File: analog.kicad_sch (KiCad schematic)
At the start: 38 parts, among them J3 Conn_02x01, J4 Conn_02x01, J5 Conn_02x01, J6 Conn_02x01, J7 Screw_Terminal_01x02, U4 ADS131A04, Y2 16.384 MHz

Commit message: June 20th is not real and cant hurt me
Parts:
- C20: renamed from C15; footprint aprlprints:C_0603-noct -> APRLPrints:C_0603
- C21: renamed from C46; footprint aprlprints:C_0603-noct -> APRLPrints:C_0603
- C22: renamed from C16; footprint aprlprints:C_0603-noct -> APRLPrints:C_0603
- C23: renamed from C17; footprint aprlprints:C_0603-noct -> APRLPrints:C_0603
- C24: renamed from C18; footprint aprlprints:C_0603-noct -> APRLPrints:C_0603
- C25: renamed from C19; footprint aprlprints:C_0603-noct -> APRLPrints:C_0603
- C26: renamed from C20; footprint aprlprints:C_0603-noct -> APRLPrints:C_0603
- C27: renamed from C21; footprint aprlprints:C_0603-noct -> APRLPrints:C_0603
- C28: renamed from C22; footprint aprlprints:C_0603-noct -> APRLPrints:C_0603
- C29: renamed from C23; footprint aprlprints:C_0603-noct -> APRLPrints:C_0603
- C30: renamed from C24; footprint aprlprints:C_0603-noct -> APRLPrints:C_0603
- C31: renamed from C25; footprint aprlprints:C_0603-noct -> APRLPrints:C_0603
- C32: renamed from C26; footprint aprlprints:C_0603-noct -> APRLPrints:C_0603
- C33: renamed from C27; footprint aprlprints:C_0603-noct -> APRLPrints:C_0603
- F2: footprint Fuse:Fuse_0805_2012Metric -> APRLPrints:Fuse_0805_2012Metric
- Y2: footprint aprlprints:3225-4P-L-noct -> APRLPrints:3225-4P-L
- renumbered U4 to U5

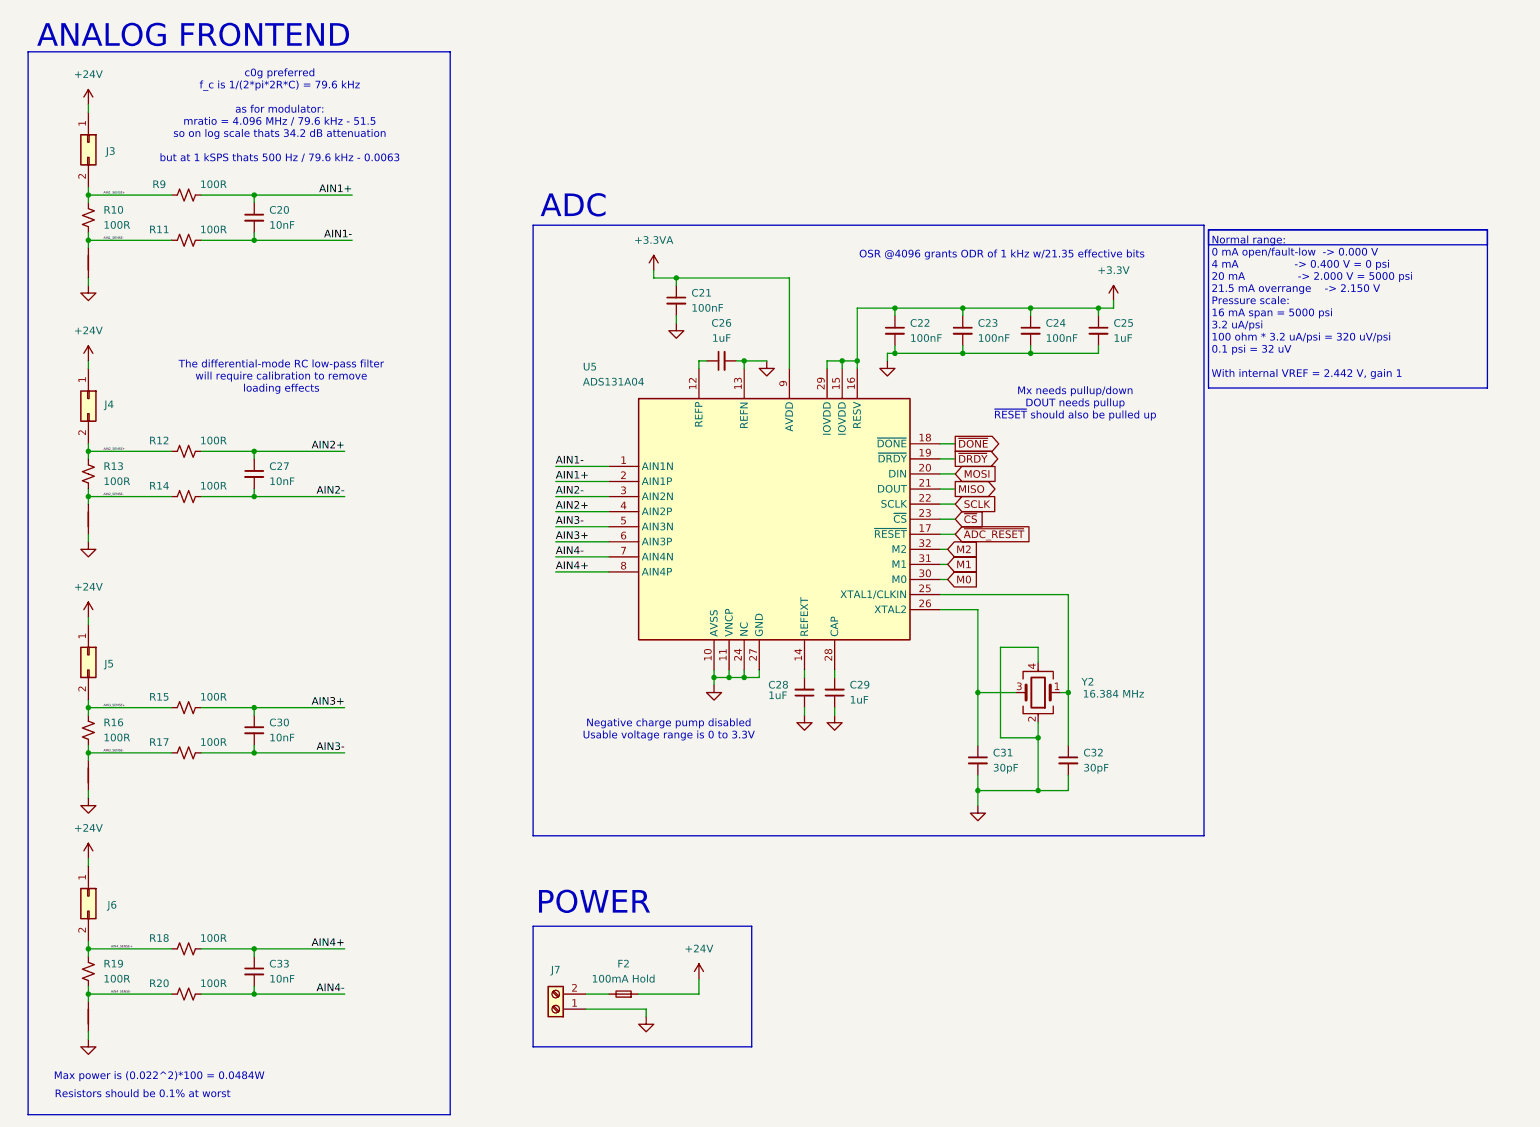
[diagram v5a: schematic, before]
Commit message: Remove LP5907
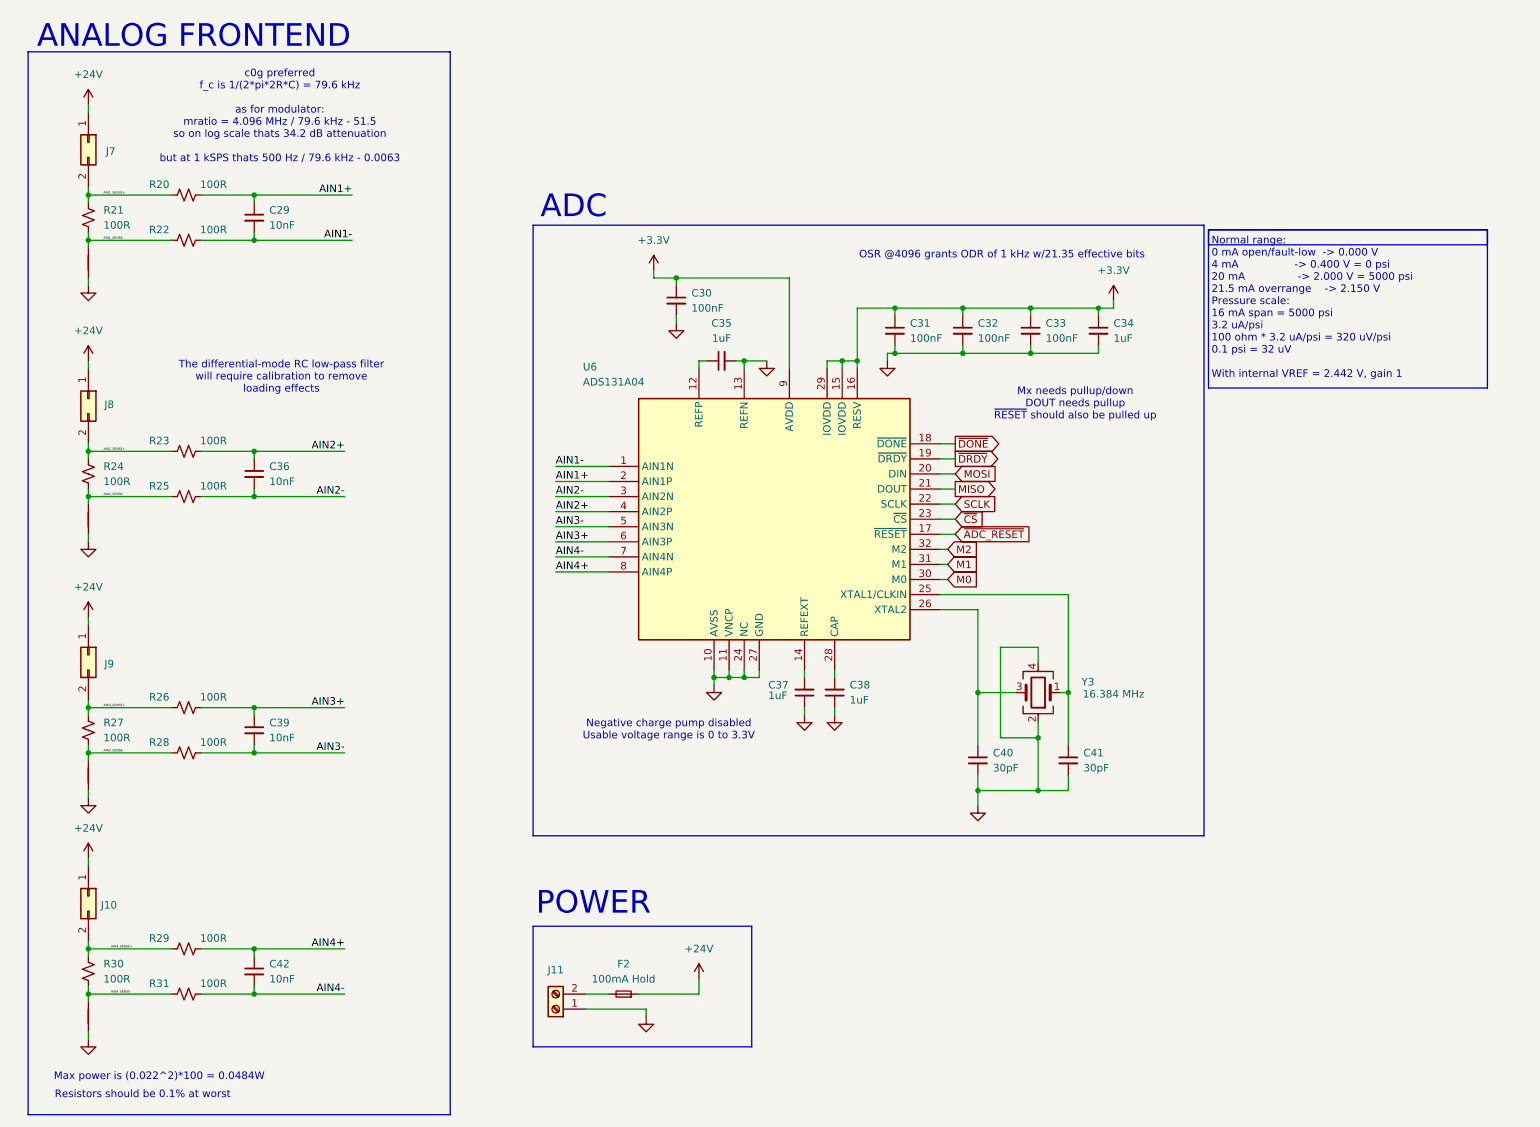
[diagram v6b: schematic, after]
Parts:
- renumbered C20 to C29, C21 to C30, C22 to C31, C23 to C32, C24 to C33, C25 to C34, C26 to C35, C27 to C36, C28 to C37, C29 to C38, C30 to C39, C31 to C40, C32 to C41, C33 to C42, J6 to J10, J7 to J11, J3 to J7, J4 to J8, J5 to J9, R9 to R20, R10 to R21, R11 to R22, R12 to R23, R13 to R24, R14 to R25, R15 to R26, R16 to R27, R17 to R28, R18 to R29, R19 to R30, R20 to R31, U5 to U6, Y2 to Y3
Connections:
- net +3.3VA is gone; now on net +3.3V: C30.1, U6.9 (AVDD)

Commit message: Use sheet pins instead of global labels where appropriate
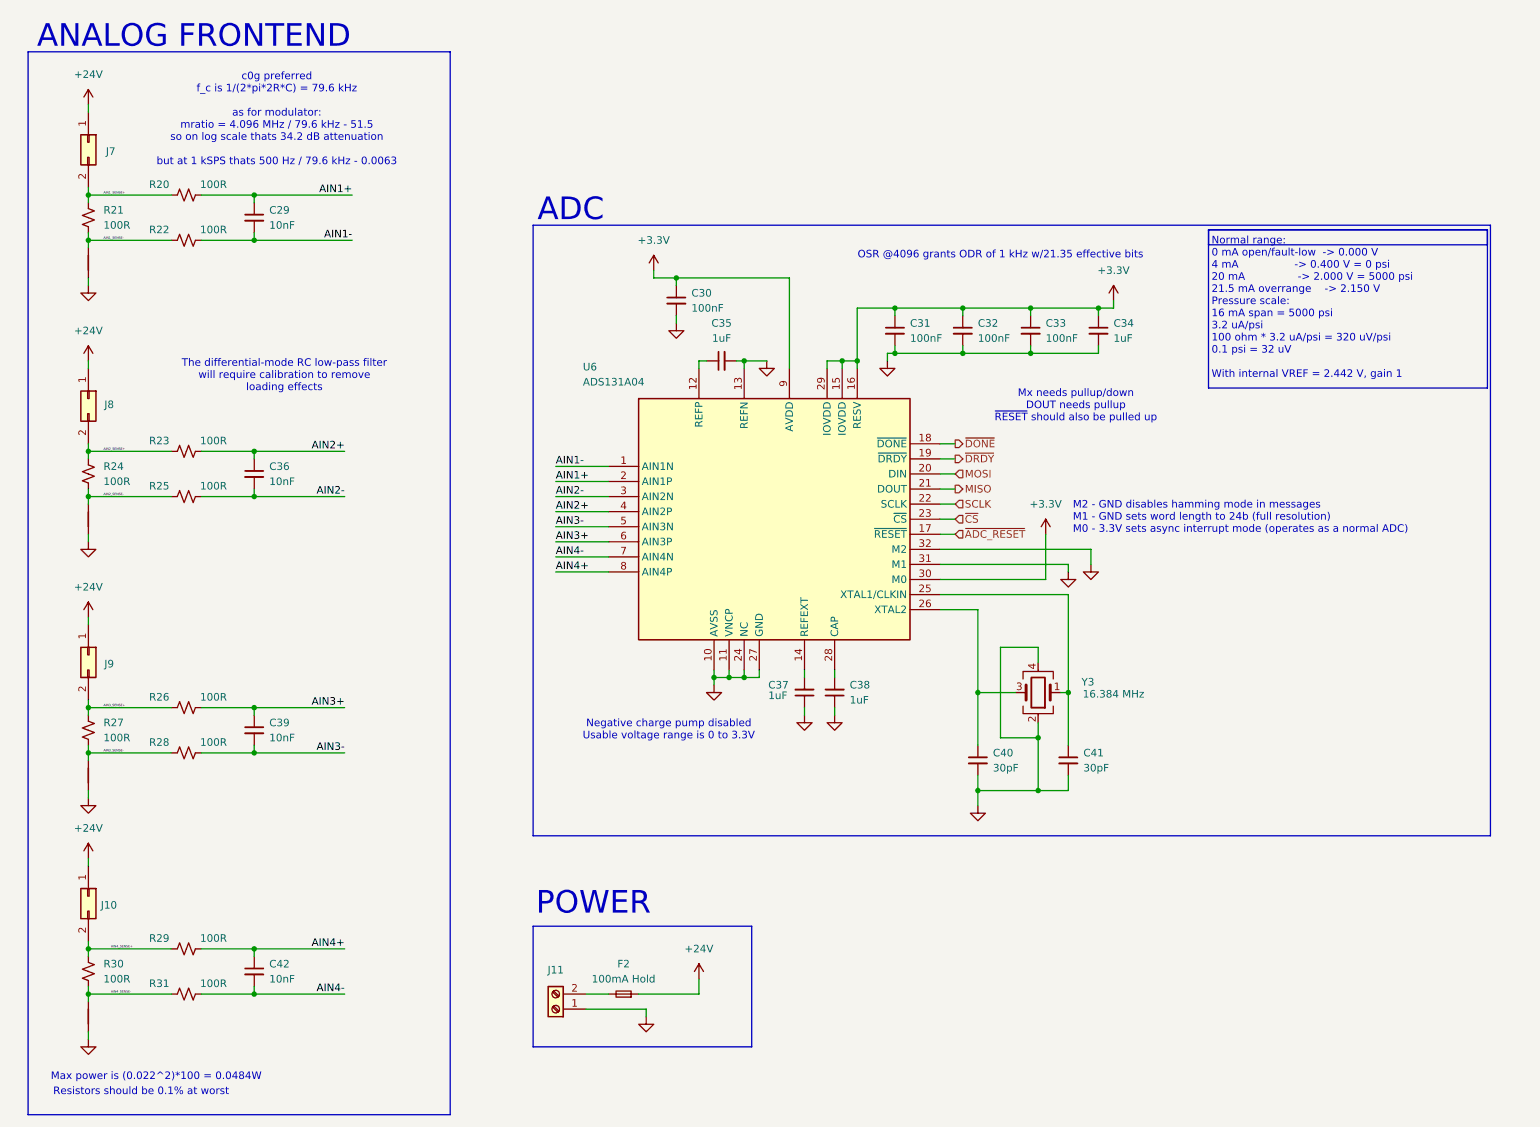
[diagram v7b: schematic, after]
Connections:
- net M0 is gone; now on net +3.3V: U6.30 (M0)
- net M1 is gone; now on net GND: U6.31 (M1)
- net M2 is gone; now on net GND: U6.32 (M2)
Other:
- note added: "M2 - GND disables hamming mode in messages M1 - GND sets word length to 24b (full resolution) M0 - 3.3V sets async interrupt mode (operates as a normal ADC)"

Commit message: holy hell 2 adcs
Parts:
- removed F2: 100mA Hold, APRLPrints:Fuse_0805_2012Metric, symbol Device:Fuse_Small
- removed J11: Screw_Terminal_01x02, TerminalBlock_Phoenix:TerminalBlock_Phoenix_MPT-0,5-2-2.54_1x02_P2.54mm_Horizontal, symbol Connector:Screw_Terminal_01x02
- renumbered J9 to J10, J10 to J11, J7 to J8, J8 to J9
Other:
- note removed: "POWER"
